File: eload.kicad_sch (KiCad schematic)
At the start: 45 parts, among them J1 Device Power, J2 Input, J3 JST Header, J4 SWD Header, J6 JST Header, Q1 TIP122, SW1 SW_Push, SW2 RotaryEncoder_Switch, U1 LM1117DT-3.3, U2 STM32F103CBT6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

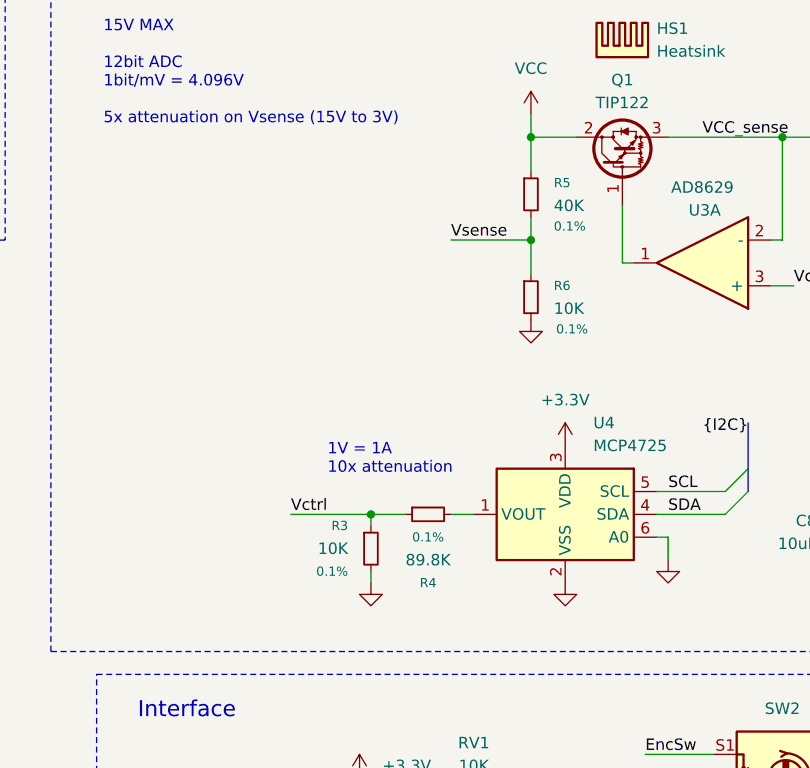
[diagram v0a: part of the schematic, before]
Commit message: Replace 89.8K resistor with 10+40+40K
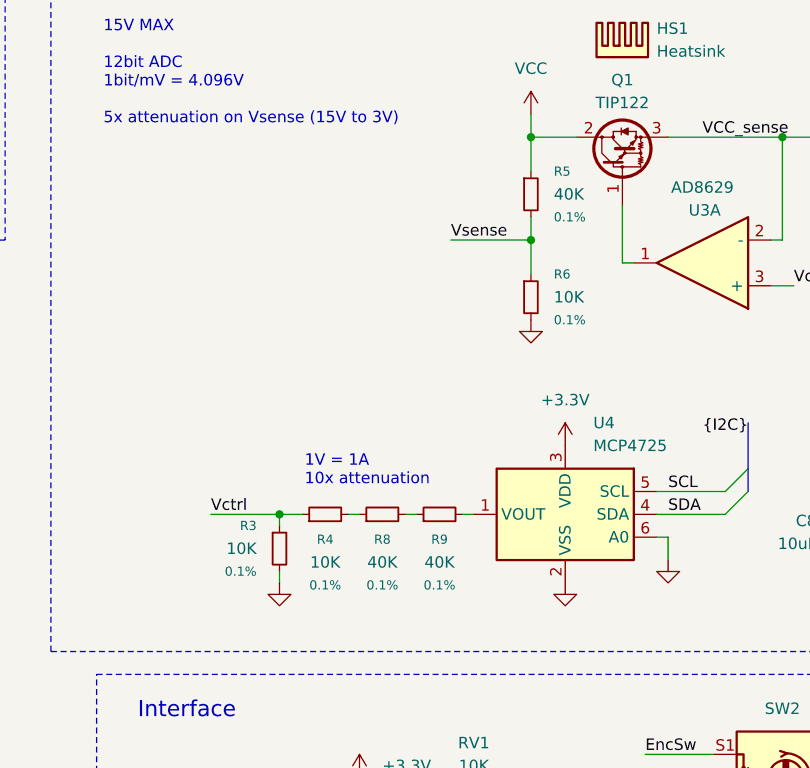
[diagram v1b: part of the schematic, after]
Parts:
- added R8, R9: 40K, Resistor_SMD:R_0805_2012Metric_Pad1.20x1.40mm_HandSolder, symbol Device:R_Small
- R4: value 89.8K -> 10K; LCSC Part # C865684 -> C110775
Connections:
- net at U4.1 (VOUT): now also R9.2; no longer R4.2
- new net: R8.2, R9.1
- new net: R4.2, R8.1
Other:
- moved on the sheet: R3

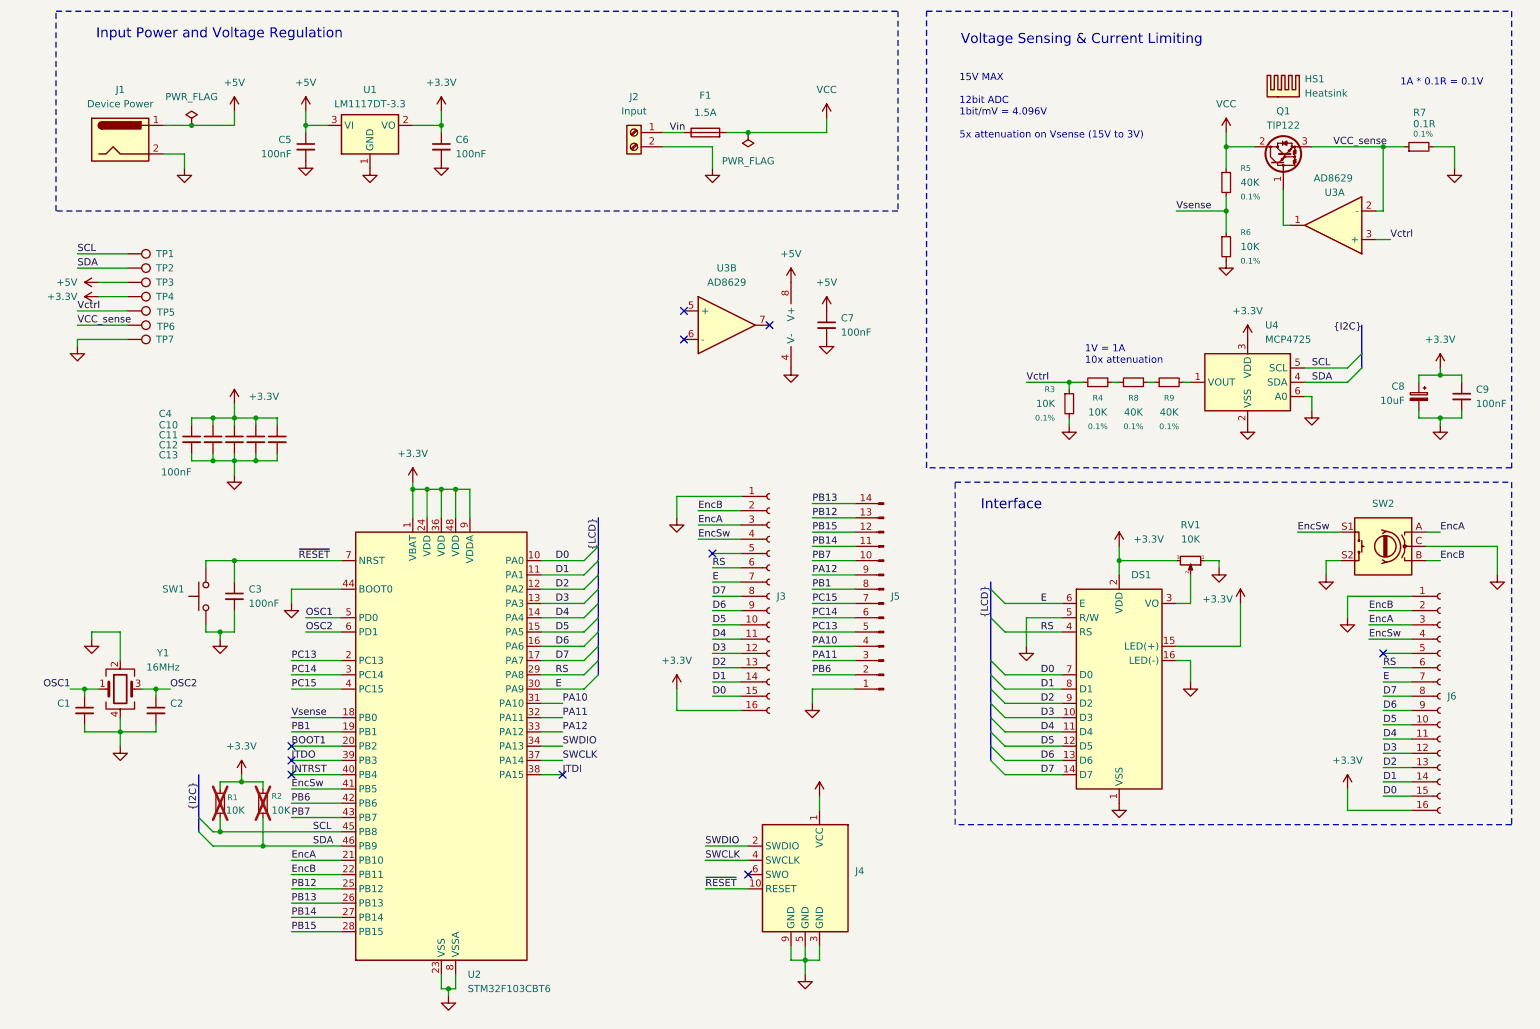
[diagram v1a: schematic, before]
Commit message: Input Relay added
OMRON G5Q-1
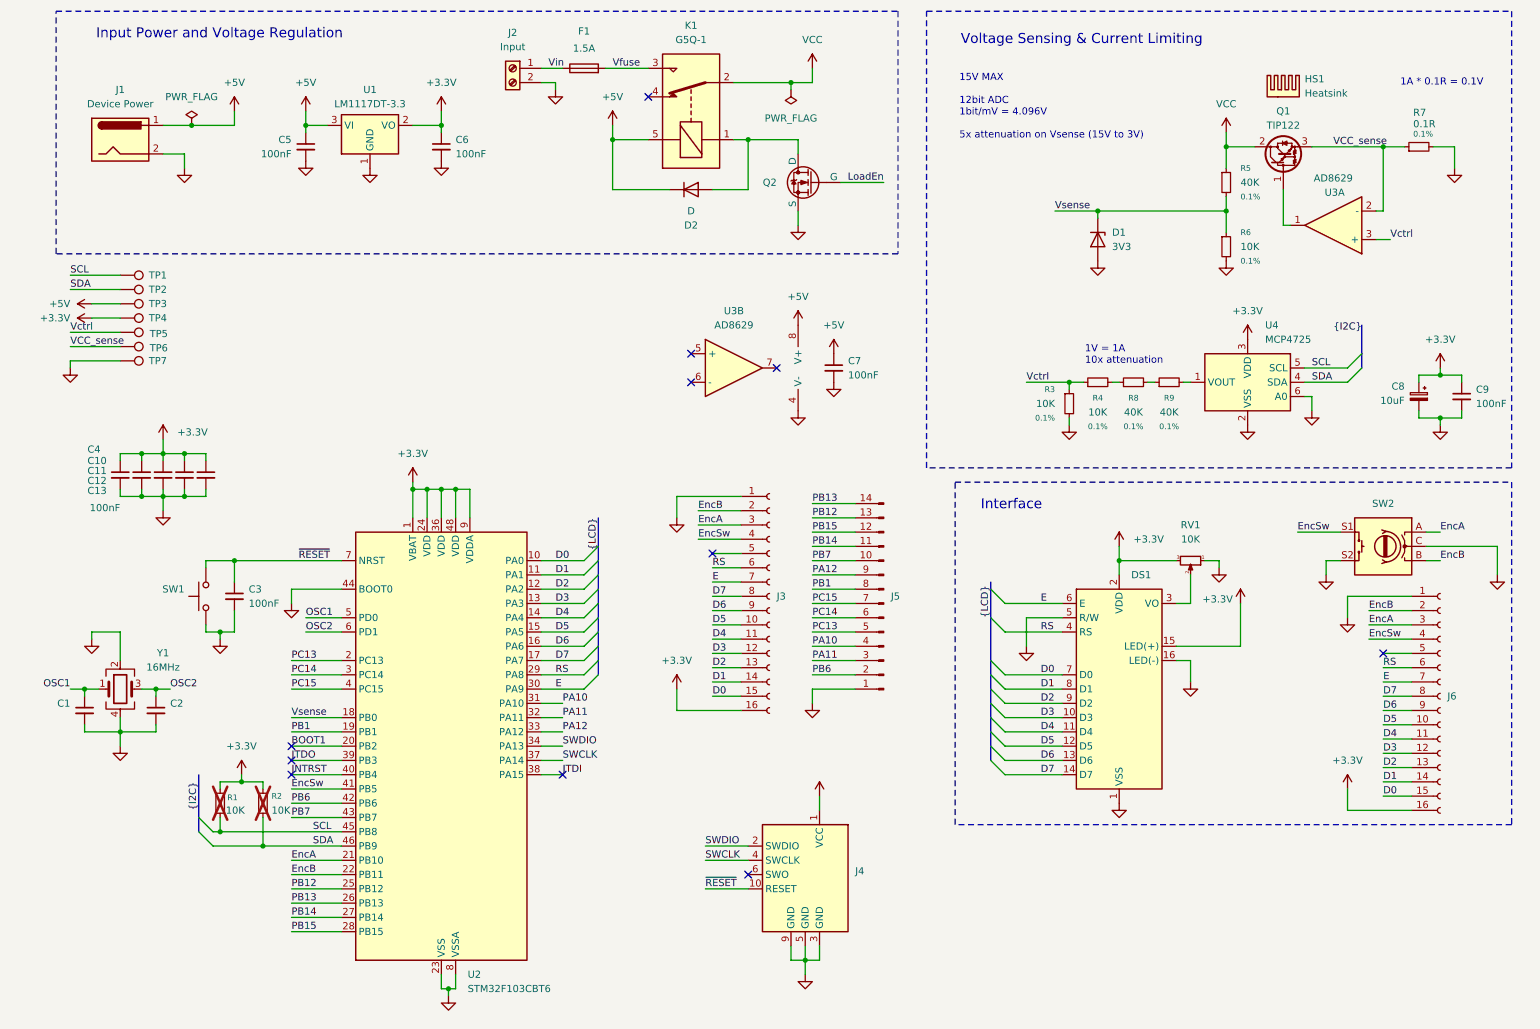
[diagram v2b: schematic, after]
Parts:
- added D1: BZT52C3V3S, Diode_SMD:D_SOD-323_HandSoldering, symbol Device:D_Zener
- added D2: D, symbol Device:D
- added K1: G5Q-1, Relay_THT:Relay_SPDT_Omron-G5Q-1, symbol Relay:G5Q-1
- added Q2: NMOS, symbol Simulation_SPICE:NMOS
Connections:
- net +5V: now also D2.1 (K), K1.5
- net GND: now also D1.2 (A), Q2.3 (S)
- net VCC: now also K1.2; no longer F1.2
- net Vsense: now also D1.1 (K)
- new net: D2.2 (A), K1.1, Q2.1 (D)
- new net LoadEn: Q2.2 (G)
- new net Vfuse: F1.2, K1.3
- no-connect marks 10 -> 11
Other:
- moved on the sheet: C10, C11, C12, C13, C4, C7, F1, J2, TP1, TP2, TP3, TP4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

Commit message: Indicator LEDs added, pin header symbol changed
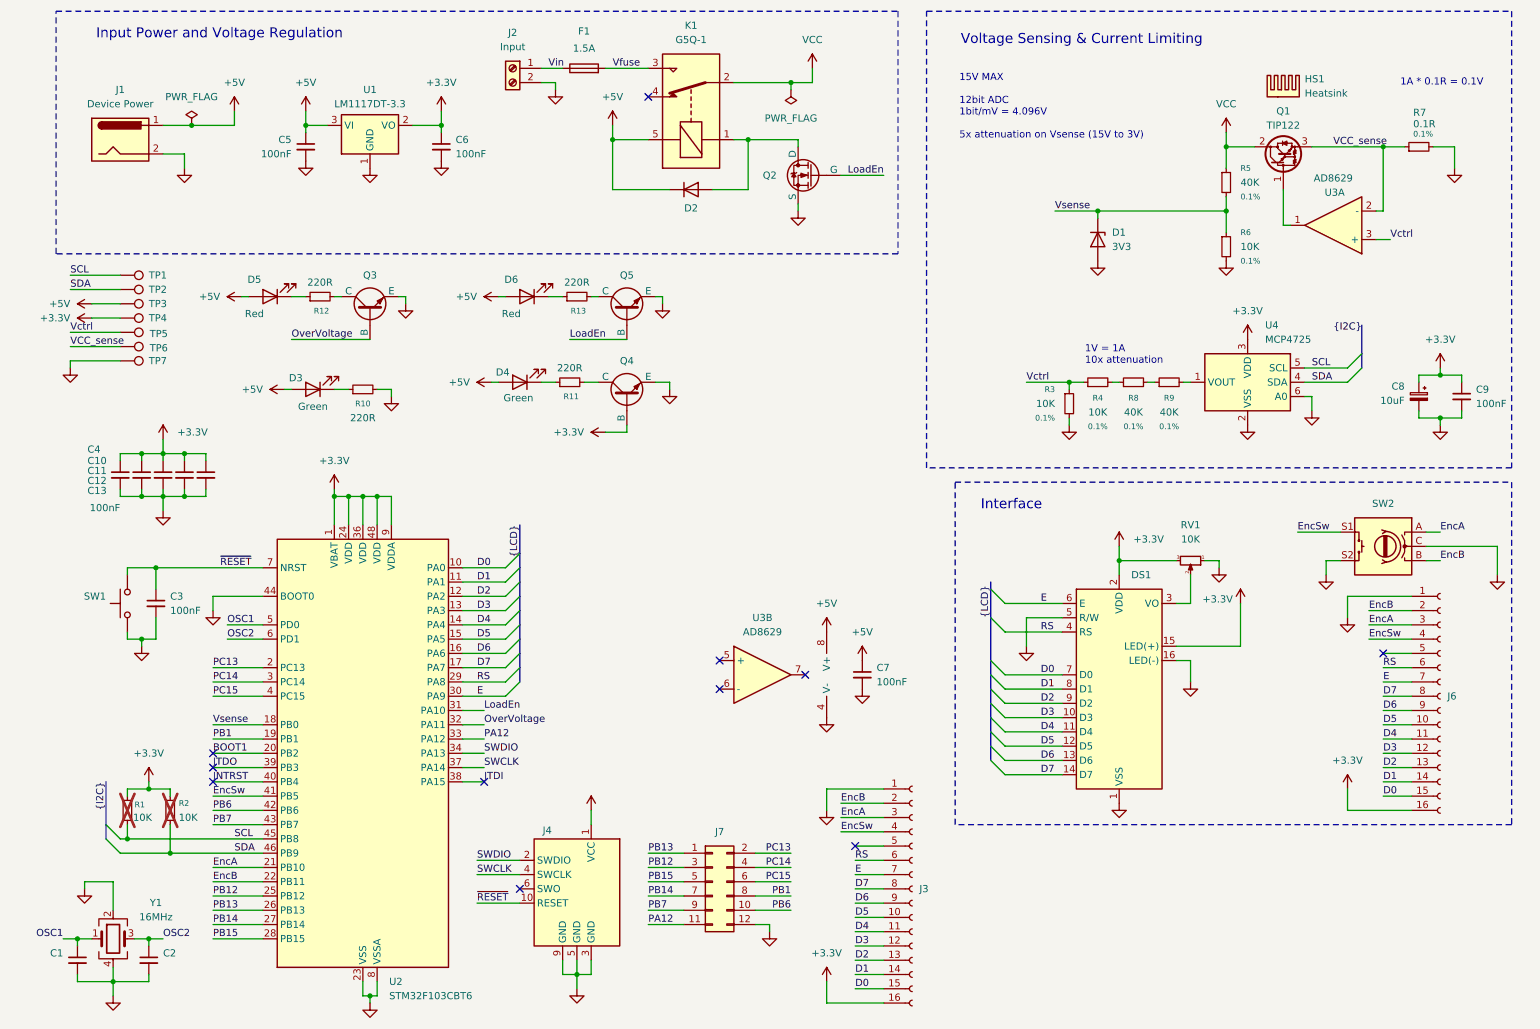
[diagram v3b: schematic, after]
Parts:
- removed J5: ~, Connector_PinHeader_2.54mm:PinHeader_2x07_P2.54mm_Vertical, symbol Connector:Conn_01x14_Pin
- added D3, D4, D5, D6: 17-215/GHC-YR1S2/4T, LED_SMD:LED_0805_2012Metric_Pad1.15x1.40mm_HandSolder, symbol Device:LED
- added J7: Conn_02x06_Odd_Even, Connector_PinHeader_2.54mm:PinHeader_2x06_P2.54mm_Vertical, symbol Connector_Generic:Conn_02x06_Odd_Even
- added Q3, Q4, Q5: DTC043Z, symbol Simulation_SPICE:NPN
- added R10, R11, R12, R13: 220R, symbol Device:R_Small
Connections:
- net PA10 is gone; now on net LoadEn: U2.31 (PA10)
- net +3.3V: now also Q4.2 (B)
- net +5V: now also D3.2 (A), D4.2 (A), D5.2 (A), D6.2 (A)
- net GND: now also J7.12 (Pin_12), Q3.3 (E), Q4.3 (E), Q5.3 (E), R10.2
- net LoadEn: now also Q5.2 (B)
- net PA12: now also J7.11 (Pin_11)
- net PB1: now also J7.8 (Pin_8)
- net PB12: now also J7.3 (Pin_3)
- net PB13: now also J7.1 (Pin_1)
- net PB14: now also J7.7 (Pin_7)
- net PB15: now also J7.5 (Pin_5)
- net PB6: now also J7.10 (Pin_10)
- net PB7: now also J7.9 (Pin_9)
- net PC13: now also J7.2 (Pin_2)
- net PC14: now also J7.4 (Pin_4)
- net PC15: now also J7.6 (Pin_6)
- net PA11 renamed OverVoltage
- net OverVoltage: now also Q3.2 (B)
- new net: D6.1 (K), R13.1
- new net: Q5.1 (C), R13.2
- new net: Q3.1 (C), R12.2
- new net: Q4.1 (C), R11.2
- new net: D4.1 (K), R11.1
- new net: D5.1 (K), R12.1
- new net: D3.1 (K), R10.1
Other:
- moved on the sheet: C1, C2, C3, C7, J3, J4, Q2, R1, R2, SW1, U2, U3B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

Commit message: Putting SWD header in a project local library
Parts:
- J4: symbol kicad:SWD Header -> eload:SWD Header
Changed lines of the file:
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@@
 	)
 	(symbol
-		(lib_id "kicad:SWD Header")
+		(lib_id "eload:SWD Header")
 		(at 118.11 165.1 0)
 		(mirror y)
